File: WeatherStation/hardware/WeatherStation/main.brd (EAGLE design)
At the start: 38 parts, among them IC1 4017N, IC2 4017N

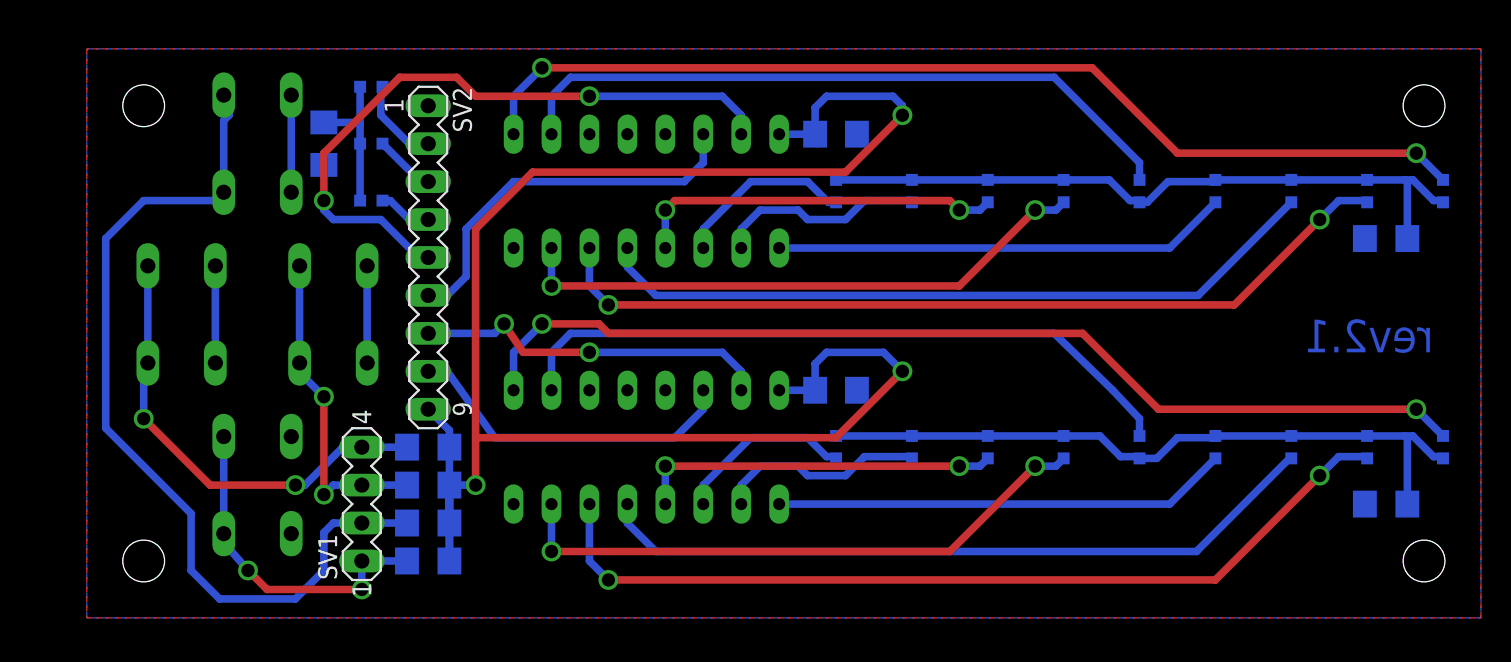
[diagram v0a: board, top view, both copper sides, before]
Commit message: SCT2167 used as a LED driver.
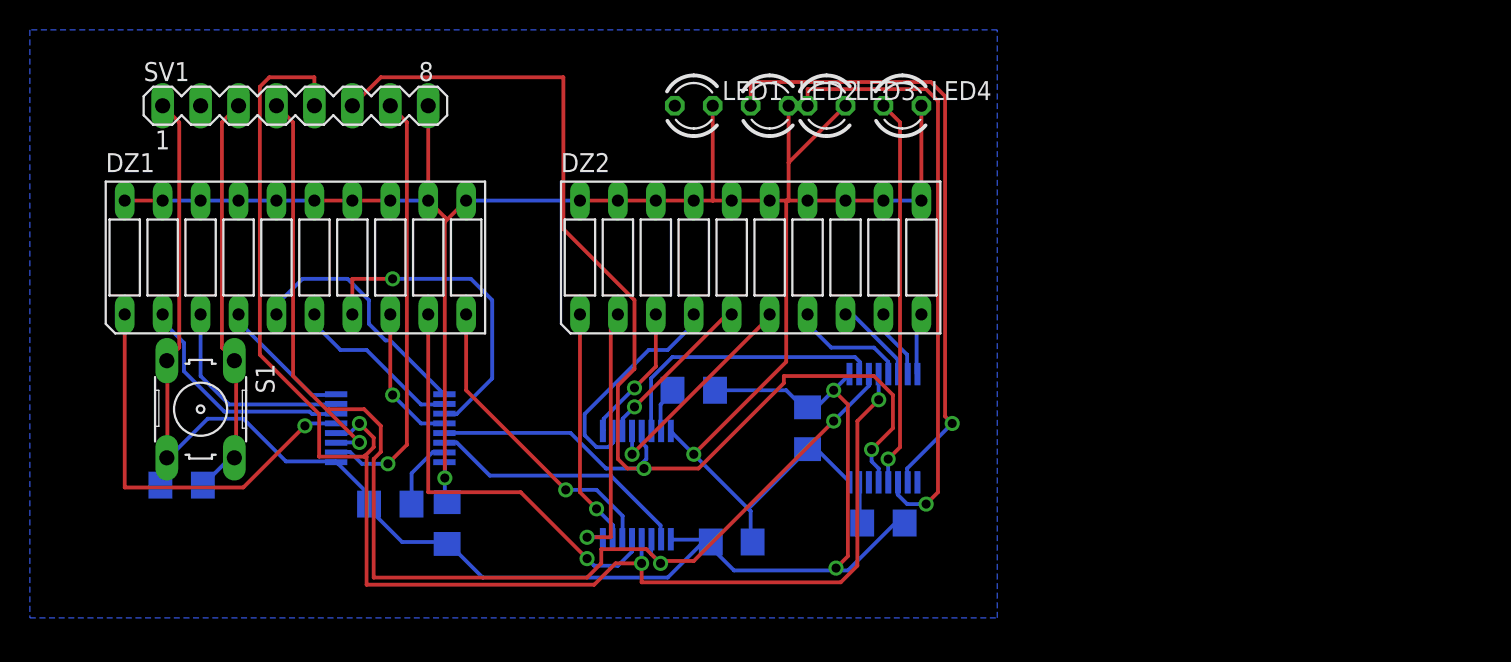
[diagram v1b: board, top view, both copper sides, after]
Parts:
- removed LED10, LED11, LED12, LED13, LED14, LED15, LED16, LED17, LED18, LED19, LED20, LED21, LED5, LED6, LED7, LED8, LED9: (no value), led:SML0603
- removed R5, R6, R7: (no value), resistor:R1206
- removed S2, S3, S4: (no value), switch-omron:B3F-10XX
- removed SV2: (no value), con-lstb:MA09-1
- added C3: (no value), resistor:C1206
- added DZ1, DZ2: LB10, led:LB10
- added IC3: SCT2167CSSG, starchips:SSOP16
- IC1, IC2: value 4017N -> SCT2167CSSG; device 40xx:DIL16 -> starchips:SSOP16
- LED1, LED2, LED3, LED4: device led:SML0603 -> led:LED3MM
- SV1: device con-lstb:MA04-1 -> con-lstb:MA08-1
- moved R1 80.7 mm to (10.2, 8.89), turned to 0 degrees
- moved R2 69.0 mm to (24.1, 7.62)
- moved C1 36.8 mm to (27.9, 6.35), turned to 270 degrees
- moved R4 30.6 mm to (57.1, 6.35), turned to 0 degrees
- moved R3 29.8 mm to (44.5, 15.2), turned to 0 degrees
- moved SV1 27.0 mm to (17.8, 34.3), turned to 0 degrees
- moved LED3 25.3 mm to (53.3, 34.3), flipped to the top, turned to 0 degrees
- moved LED4 25.3 mm to (58.4, 34.3), flipped to the top, turned to 0 degrees
- moved LED1 24.8 mm to (44.5, 34.3), flipped to the top, turned to 0 degrees
- moved LED2 24.8 mm to (49.5, 34.3), flipped to the top, turned to 0 degrees
- moved IC2 19.7 mm to (40.6, 8.89)
- moved IC1 17.2 mm to (24.1, 12.7), turned to 90 degrees
- moved C2 12.3 mm to (47.0, 5.08), turned to 0 degrees
- moved S1 6.48 mm to (11.4, 14.0), flipped to the top
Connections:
- removed net N$1: LED1.C, LED2.C, LED3.C, LED4.C, LED5.C, LED6.C, LED7.C, LED8.C, LED9.C, R1.2
- removed net N$10: IC1.9, LED9.A
- removed net N$11: LED10.C, LED11.C, LED12.C, LED13.C, LED14.C, LED15.C, LED16.C, LED17.C, LED18.C, R2.2
- removed net N$12: IC2.3, LED10.A
- removed net N$14: IC2.4, LED12.A
- removed net N$15: IC2.7, LED13.A
- removed net N$16: IC2.1, LED15.A
- removed net N$18: IC2.6, LED17.A
- removed net N$19: IC2.9, LED18.A
- removed net N$2: IC1.3, LED1.A
- removed net N$20: IC2.10, LED14.A
- removed net N$21: IC1.14, SV2.8
- removed net N$22: IC1.15, SV2.7
- removed net N$23: LED19.C, LED20.C, LED21.C, R3.2
- removed net N$24: LED19.A, SV2.2
- removed net N$25: LED20.A, SV2.3
- removed net N$26: LED21.A, SV2.4
- removed net N$27: IC2.15, SV2.5
- removed net N$28: IC2.14, SV2.6
- removed net N$29: R7.1, S1.1, S1.2, SV1.4
- removed net N$30: R6.1, S2.1, S2.2, SV1.3
- removed net N$31: R5.1, S3.1, S3.2, SV1.2
- removed net N$32: R4.1, S4.1, S4.2, SV1.1
- removed net N$5: IC1.7, LED4.A
- removed net N$6: IC1.10, LED5.A
- removed net N$7: IC1.1, LED6.A
- removed net N$9: IC1.6, LED8.A
- new net CU-CLK: IC1.3, IC2.3, IC3.3, SV1.4
- new net CU-CTRL: R1.1, S1.1, S1.2, SV1.3
- new net CU-LA: IC1.4, IC2.4, IC3.4, SV1.5
- new net CU-OE: IC1.13, IC2.13, IC3.13, SV1.6
- new net CU-SDI: IC1.2, SV1.7
- new net DZ1-1: DZ1.1, IC1.5
- new net DZ1-10: DZ1.10, IC2.6
- new net DZ1-2: DZ1.2, IC1.6
- new net DZ1-3: DZ1.3, IC1.7
- new net DZ1-4: DZ1.4, IC1.8
- new net DZ1-5: DZ1.5, IC1.9
- new net DZ1-6: DZ1.6, IC1.10
- new net DZ1-7: DZ1.7, IC1.11
- new net DZ1-8: DZ1.8, IC1.12
- new net DZ1-9: DZ1.9, IC2.5
- new net DZ2-1: DZ2.1, IC2.7
- new net DZ2-10: DZ2.10, IC3.8
- new net DZ2-2: DZ2.2, IC2.8
- new net DZ2-3: DZ2.3, IC2.9
- new net DZ2-4: DZ2.4, IC2.10
- new net DZ2-5: DZ2.5, IC2.11
- new net DZ2-6: DZ2.6, IC2.12
- new net DZ2-7: DZ2.7, IC3.5
- new net DZ2-8: DZ2.8, IC3.6
- new net DZ2-9: DZ2.9, IC3.7
- new net LED-MODE-1: LED1.A
- new net LED-MODE-2: IC3.10, LED2.A
- new net LED-MODE-3: IC3.11, LED3.A
- new net LED-MODE-4: IC3.12, LED4.A
- net GND: now also C3.2, IC1.1, IC2.1, IC3.1, R4.1, SV1.1; no longer IC1.13, IC1.8, IC2.13, IC2.8, R1.1, S2.3, S2.4, S3.3, S3.4, S4.3, S4.4, SV2.1
- net N$13: now also IC2.15, R3.2; no longer IC2.2, LED11.A
- net N$17: now also IC3.15, R4.2; no longer IC2.5, LED16.A
- net N$3: now also IC1.14, IC2.2; no longer IC1.2, LED2.A
- net N$4: now also IC2.14, IC3.2; no longer IC1.4, LED3.A
- net N$8: now also IC1.15, R2.2; no longer IC1.5, LED7.A
- net VCC: now also C3.1, DZ1.11, DZ1.12, DZ1.13, DZ1.14, DZ1.15, DZ1.16, DZ1.17, DZ1.18, DZ1.19, DZ1.20, DZ2.11, DZ2.12, DZ2.13, DZ2.14, DZ2.15, DZ2.16, DZ2.17, DZ2.18, DZ2.19, DZ2.20, IC3.16, LED1.K, LED2.K, LED3.K, LED4.K, R1.2, SV1.8; no longer R4.2, R5.2, R6.2, R7.2, SV2.9
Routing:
- net CU-LA: track 0.00 -> 98.9 mm, vias 0 -> 3
- net GND: track 19.5 -> 110.3 mm, vias 0 -> 2
- net CU-OE: track 0.00 -> 88.7 mm, vias 0 -> 2
- net CU-CLK: track 0.00 -> 83.4 mm, vias 0 -> 3
- net N$19: track 68.7 -> 0.00 mm, vias 2 -> 0
- net N$10: track 68.7 -> 0.00 mm, vias 2 -> 0
- net N$9: track 59.9 -> 0.00 mm, vias 2 -> 0
- net N$31: track 59.5 -> 0.00 mm
- net N$18: track 58.1 -> 0.00 mm, vias 2 -> 0
- net N$1: track 47.1 -> 0.00 mm
- net N$11: track 46.5 -> 0.00 mm
- net N$17: track 49.1 -> 2.82 mm
- net N$6: track 46.0 -> 0.00 mm
- net N$20: track 46.0 -> 0.00 mm
- net N$27: track 44.5 -> 0.00 mm, vias 2 -> 0
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- added copper zone on layer 16, net N$1
- removed copper zone on layer 1, net GND
- removed copper zone on layer 16, net GND
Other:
- board text removed: "rev2.1"

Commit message: 7 Segment LED Display project added.
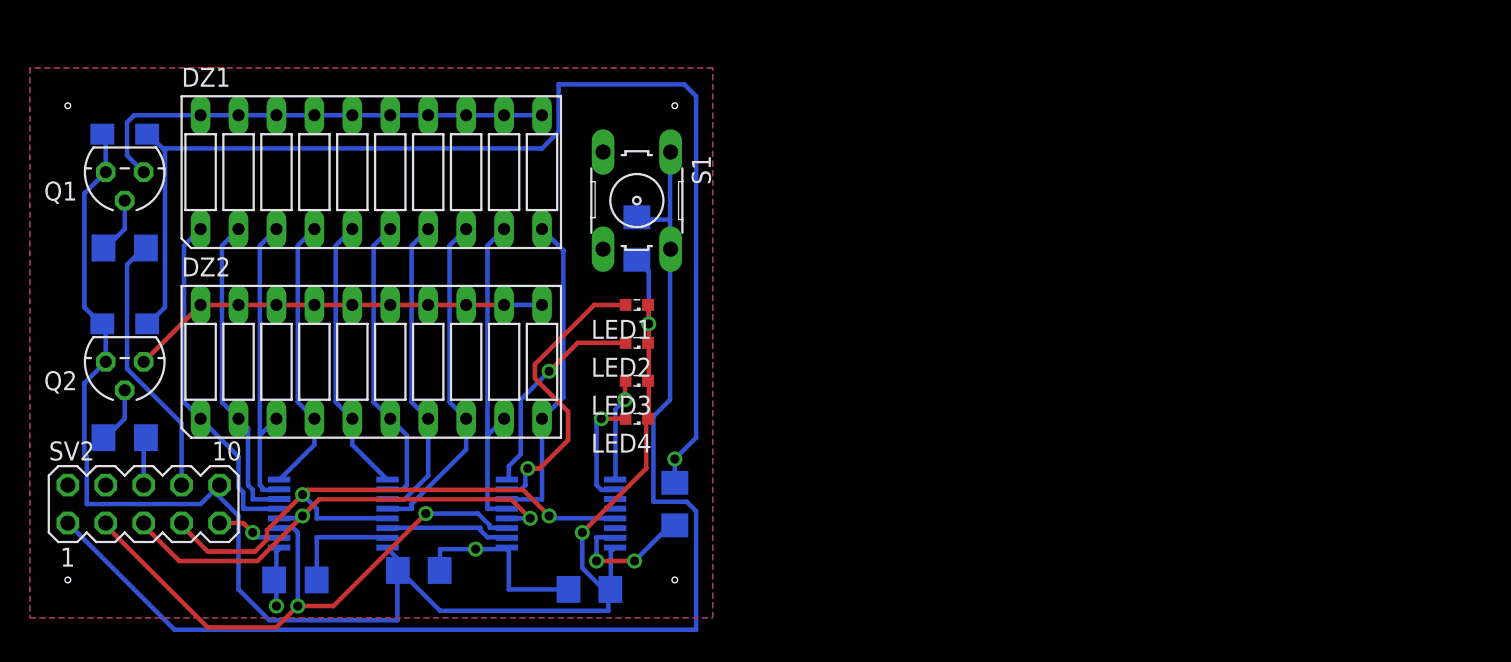
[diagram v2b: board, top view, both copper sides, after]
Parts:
- removed IC3: SCT2167CSSG, starchips:SSOP16
- removed SV1: (no value), con-lstb:MA08-1
- added C4: 1u, resistor:SMC_A
- added Q1, Q2: BC327, transistor-pnp:TO92
- added R5: 1k, resistor:R1206
- added SV2: (no value), con-lstb:MA05-2
- C1, C2: value (none) -> 100n
- C3: value (none) -> 1u; device resistor:C1206 -> resistor:SMC_A
- LED1, LED2, LED3, LED4: device led:LED3MM -> led:SML0603
- R1, R2, R3, R4: value (none) -> 1k
- moved R4 54.0 mm to (6.35, 24.8), turned to 180 degrees
- moved C3 49.8 mm to (6.35, 32.4), turned to 180 degrees
- moved R1 34.7 mm to (40.6, 25.4), turned to 270 degrees
- moved S1 32.4 mm to (40.6, 27.9)
- moved LED4 27.5 mm to (40.6, 13.3), turned to 180 degrees
- moved DZ2 26.3 mm to (22.9, 17.1)
- moved LED3 22.4 mm to (40.6, 15.9), turned to 180 degrees
- moved LED2 18.2 mm to (40.6, 18.4), turned to 180 degrees
- moved LED1 13.9 mm to (40.6, 21.0), turned to 180 degrees
- moved C2 10.0 mm to (37.5, 1.91)
- moved R2 8.13 mm to (17.8, 2.54)
- moved R3 7.73 mm to (43.2, 7.62), turned to 270 degrees
- moved DZ1 7.65 mm to (22.9, 29.8)
- moved IC1 6.87 mm to (20.3, 6.99)
- moved IC2 5.43 mm to (35.6, 6.99), turned to 90 degrees
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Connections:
- removed net DZ1-1: DZ1.1, IC1.5
- removed net DZ1-10: DZ1.10, IC2.6
- removed net DZ1-2: DZ1.2, IC1.6
- removed net DZ1-3: DZ1.3, IC1.7
- removed net DZ1-4: DZ1.4, IC1.8
- removed net DZ1-5: DZ1.5, IC1.9
- removed net DZ1-6: DZ1.6, IC1.10
- removed net DZ1-7: DZ1.7, IC1.11
- removed net DZ1-8: DZ1.8, IC1.12
- removed net DZ1-9: DZ1.9, IC2.5
- removed net DZ2-1: DZ2.1, IC2.7
- removed net DZ2-10: DZ2.10, IC3.8
- removed net DZ2-2: DZ2.2, IC2.8
- removed net DZ2-3: DZ2.3, IC2.9
- removed net DZ2-4: DZ2.4, IC2.10
- removed net DZ2-5: DZ2.5, IC2.11
- removed net DZ2-6: DZ2.6, IC2.12
- removed net DZ2-7: DZ2.7, IC3.5
- removed net DZ2-8: DZ2.8, IC3.6
- removed net DZ2-9: DZ2.9, IC3.7
- removed net LED-MODE-1: LED1.A
- removed net LED-MODE-2: IC3.10, LED2.A
- removed net LED-MODE-3: IC3.11, LED3.A
- removed net LED-MODE-4: IC3.12, LED4.A
- removed net N$17: IC3.15, R4.2
- new net LED1: DZ1.1, DZ2.1, IC1.5
- new net LED10: DZ1.10, DZ2.10, IC2.6
- new net LED11: IC2.7, LED1.A
- new net LED12: IC2.8, LED2.A
- new net LED13: IC2.9, LED3.A
- new net LED14: IC2.10, LED4.A
- new net LED2: DZ1.2, DZ2.2, IC1.6
- new net LED3: DZ1.3, DZ2.3, IC1.7
- new net LED4: DZ1.4, DZ2.4, IC1.8
- new net LED5: DZ1.5, DZ2.5, IC1.9
- new net LED6: DZ1.6, DZ2.6, IC1.10
- new net LED7: DZ1.7, DZ2.7, IC1.11
- new net LED8: DZ1.8, DZ2.8, IC1.12
- new net LED9: DZ1.9, DZ2.9, IC2.5
- new net MUL1: R4.2, SV2.8
- new net MUL2: R5.2, SV2.6
- new net N$2: DZ1.11, DZ1.12, DZ1.13, DZ1.14, DZ1.15, DZ1.16, DZ1.17, DZ1.18, DZ1.19, DZ1.20, Q1.3
- new net N$5: DZ2.11, DZ2.12, DZ2.13, DZ2.14, DZ2.15, DZ2.16, DZ2.17, DZ2.18, DZ2.19, DZ2.20, Q2.3
- new net N$6: Q2.2, R5.1
- net CU-CLK: now also SV2.3; no longer IC3.3, SV1.4
- net CU-CTRL: now also SV2.1; no longer SV1.3
- net CU-LA: now also SV2.5; no longer IC3.4, SV1.5
- net CU-OE: now also SV2.7; no longer IC3.13, SV1.6
- net CU-SDI: now also SV2.9; no longer SV1.7
- net GND: now also C3.-, C4.-, SV2.2; no longer C3.2, IC3.1, R4.1, SV1.1
- net N$4: now also Q1.2, R4.1; no longer IC2.14, IC3.2
- net VCC: now also C3.+, C4.+, LED1.C, LED2.C, LED3.C, LED4.C, Q1.1, Q2.1, SV2.10; no longer C3.1, DZ1.11, DZ1.12, DZ1.13, DZ1.14, DZ1.15, DZ1.16, DZ1.17, DZ1.18, DZ1.19, DZ1.20, DZ2.11, DZ2.12, DZ2.13, DZ2.14, DZ2.15, DZ2.16, DZ2.17, DZ2.18, DZ2.19, DZ2.20, IC3.16, LED1.K, LED2.K, LED3.K, LED4.K, SV1.8
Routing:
- net CU-LA: track 98.9 -> 32.5 mm, vias 3 -> 2
- net CU-CTRL: track 27.4 -> 82.4 mm
- net CU-OE: track 88.7 -> 39.6 mm
- net CU-CLK: track 83.4 -> 39.8 mm, vias 3 -> 2
- net LED-MODE-2: track 42.3 -> 0.00 mm, vias 1 -> 0
- net LED-MODE-3: track 40.5 -> 0.00 mm, vias 1 -> 0
- net VCC: track 144.1 -> 107.5 mm
- net N$2: track 0.00 -> 31.8 mm
- net DZ1-9: track 28.8 -> 0.00 mm, vias 1 -> 0
- net N$5: track 0.00 -> 28.2 mm
- net DZ1-1: track 27.5 -> 0.00 mm, vias 1 -> 0
- net LED-MODE-4: track 26.0 -> 0.00 mm, vias 1 -> 0
- net CU-SDI: track 28.8 -> 4.60 mm
- net LED1: track 0.00 -> 23.2 mm
- net LED8: track 0.00 -> 22.8 mm
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- added copper zone on layer 1, net GND
